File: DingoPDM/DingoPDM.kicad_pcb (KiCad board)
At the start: 4 copper layers, 72.4 x 95.2 mm, 156 parts, among them J1 RedCubeTerminal, J2 RedCubeTerminal, J3 Conn_01x12, J4 TC, J5 USB_C_Receptacle_USB2.0, SW1 BOOT, U1 VXO7805-500-M, U10 BTS7008-2EPA, U11 BTS7008-2EPA, U12 LM324, U13 BTS7008-2EPA, U14 OKI-78SR-5_1.5-W36H-C, U15 TSR_1-2450, U2 LD1117S33CTR, U3 PCA82C250, U4 STM32F446RETx, U5 MB85RC256V, U6 MCP9808, U7 LM324, U8 BTS700n-1EPP, U9 BTS700n-1EPP, Y1 8mHz

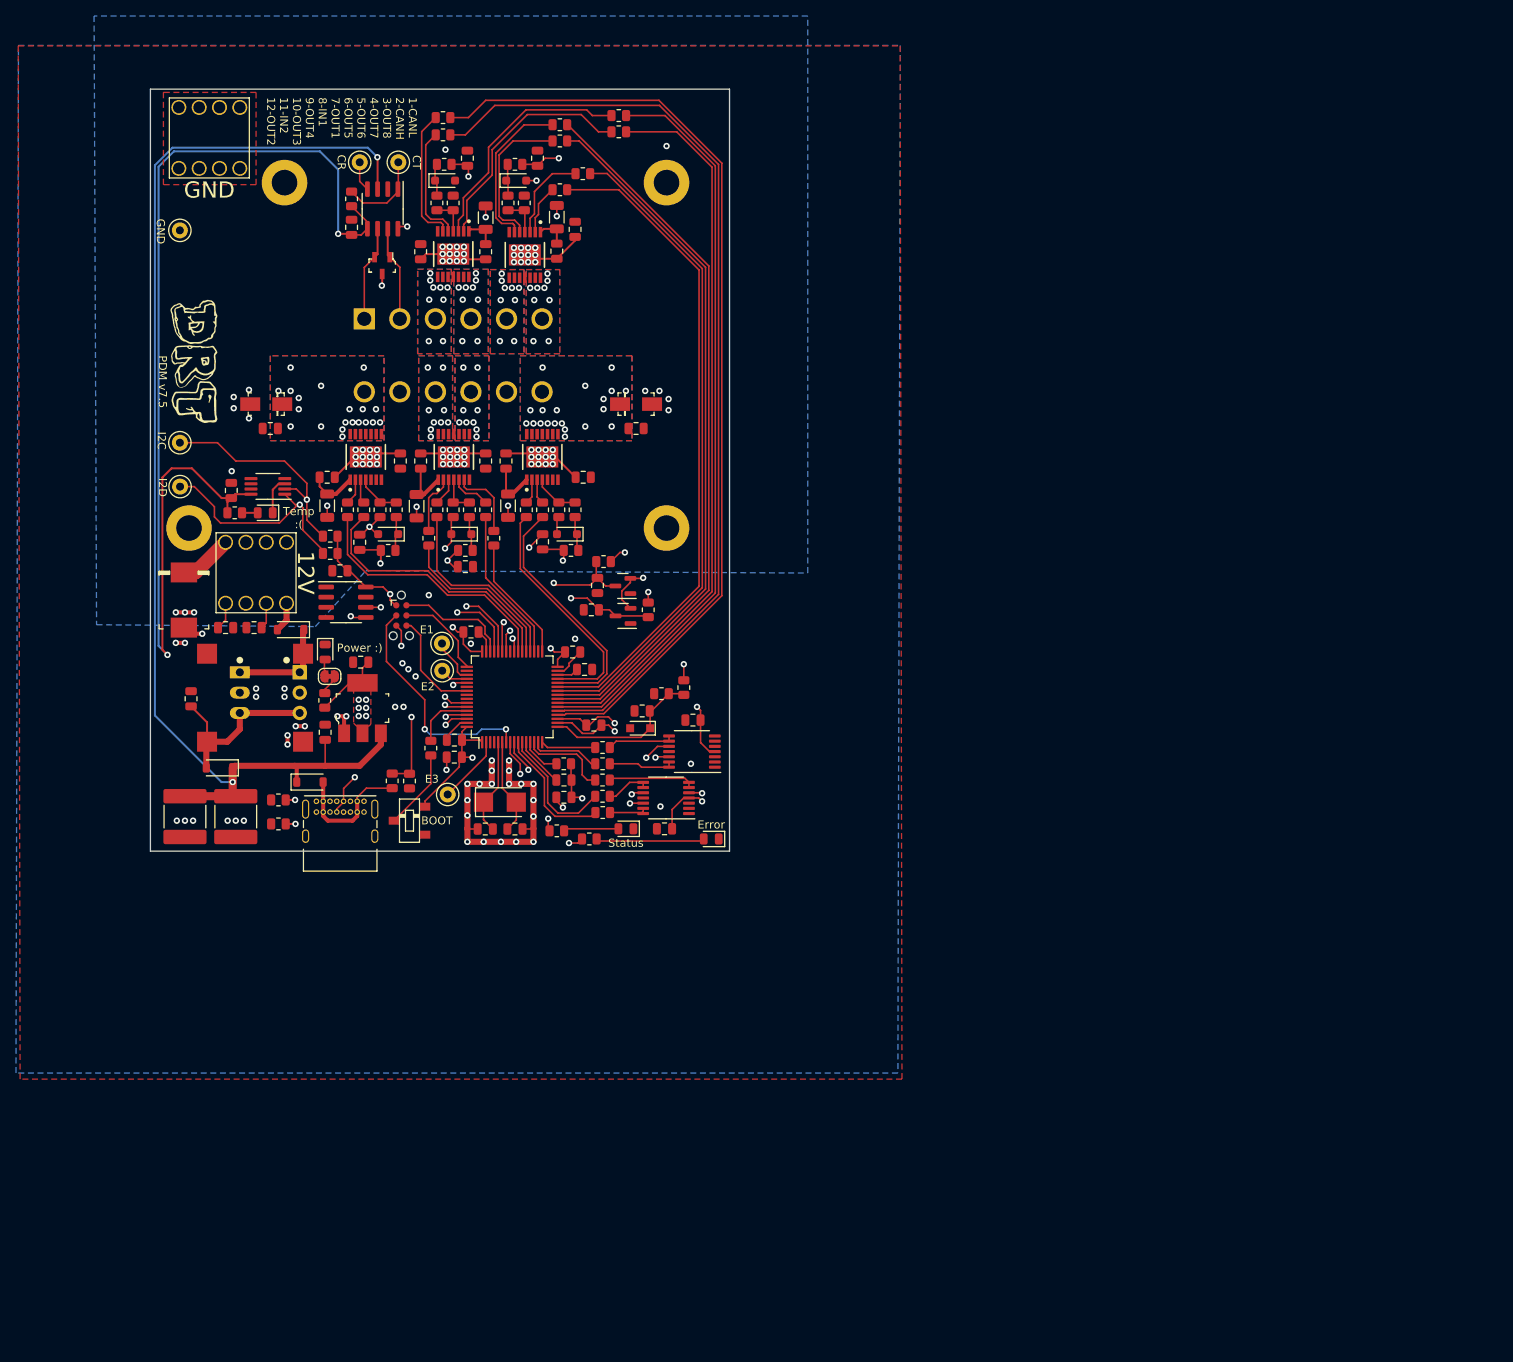
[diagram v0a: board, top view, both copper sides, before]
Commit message: Modified PCB for 10ch PDM board
I modified the original dingoPDM for 10 channels. The board has been manufactured, tested and works but after mounting I decided that it doesn't suit my needs for the current build. I may develop it further in the future, make it pretty etc but for now I am marking this project as stale.
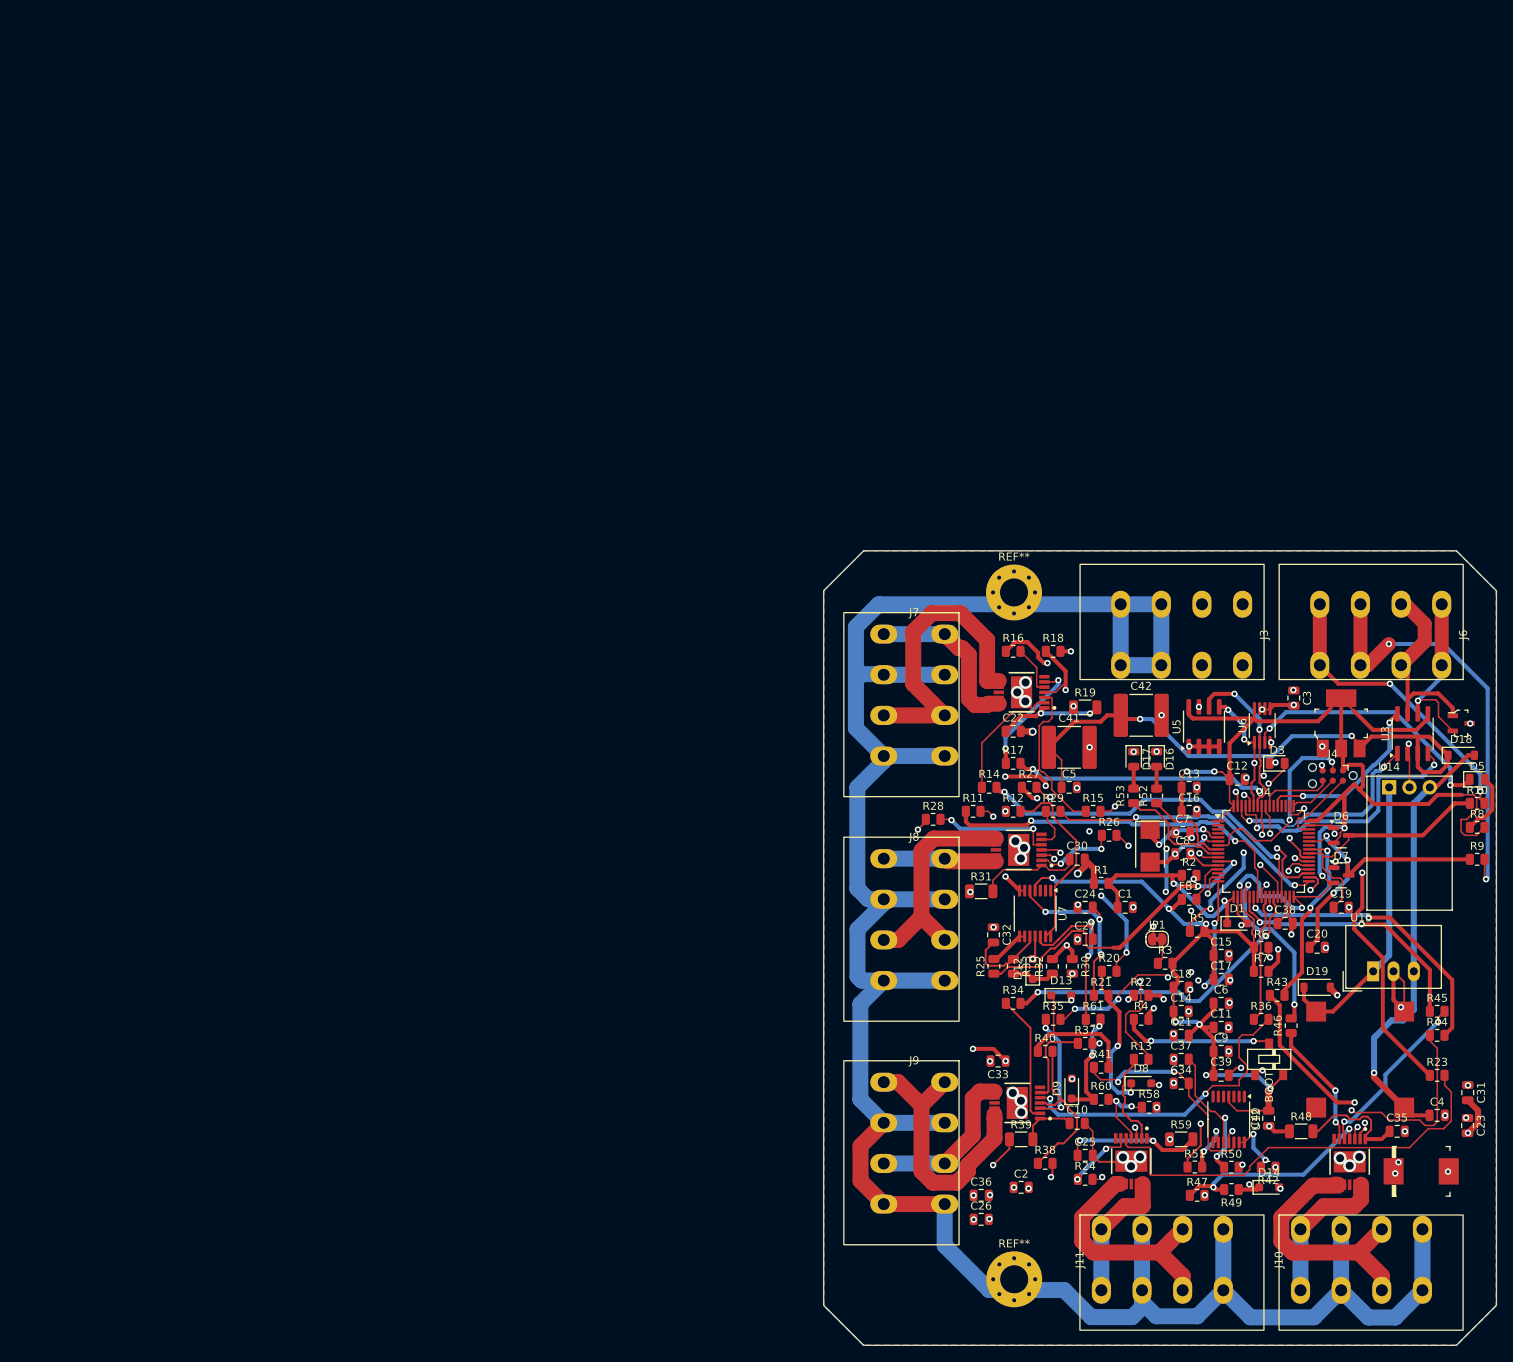
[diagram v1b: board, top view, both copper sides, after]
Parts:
- removed C28: 10nF, Capacitor_SMD:C_0805_2012Metric
- removed C29: 220pF, Capacitor_SMD:C_0805_2012Metric
- removed D10: BYG23M, dingoPDM:DO-214AC
- removed D11: 3.3V, Diode_SMD:D_SOD-323_HandSoldering
- removed D15: Schottky, Diode_SMD:D_SOD-123
- removed G1: DRT_Logo, dingoPDM:DRTLogo
- removed G2: DingoFace, dingoPDM:DingoFaceNoFill
- removed H1, H2, H3, H4: M3, MountingHole:MountingHole_3.2mm_M3_ISO7380_Pad
- removed J1, J2: RedCubeTerminal, dingoPDM:M6_Hole_8Pin_7461084
- removed J5: USB_C_Receptacle_USB2.0, Connector_USB:USB_C_Receptacle_GCT_USB4085
- removed R54, R55: 5.1K, Resistor_SMD:R_0805_2012Metric
- removed R56: 4.7K, Resistor_SMD:R_0805_2012Metric
- removed R57: 10K, Resistor_SMD:R_0805_2012Metric
- removed TP1: GND, TestPoint:TestPoint_Keystone_5000-5004_Miniature
- removed TP10: E3, TestPoint:TestPoint_Keystone_5000-5004_Miniature
- removed TP2: CAN_T, TestPoint:TestPoint_Keystone_5000-5004_Miniature
- removed TP3: CAN_R, TestPoint:TestPoint_Keystone_5000-5004_Miniature
- removed TP5: I2C1_SCL, TestPoint:TestPoint_Keystone_5000-5004_Miniature
- removed TP6: I2C1_SDA, TestPoint:TestPoint_Keystone_5000-5004_Miniature
- removed TP8: E1, TestPoint:TestPoint_Keystone_5000-5004_Miniature
- removed TP9: E2, TestPoint:TestPoint_Keystone_5000-5004_Miniature
- added J10: out7_8, DF_Conn:DIP-8_300_ELL, F.Cu at (113.5, 113.1)
- added J11: out9_10, DF_Conn:DIP-8_300_ELL, F.Cu at (88.6, 113.1)
- added J6: conn_comms, DF_Conn:DIP-8_300_ELL, F.Cu at (116.0, 34.9)
- added J7: out1_2, DF_Conn:DIP-8_300_ELL, F.Cu at (57.6, 42.5)
- added J8: out3_4, DF_Conn:DIP-8_300_ELL, F.Cu at (57.6, 70.5)
- added J9: out5_6, DF_Conn:DIP-8_300_ELL, F.Cu at (57.6, 98.5)
- added R58: 1.2K, Resistor_SMD:R_0805_2012Metric, F.Cu at (87.0, 94.0)
- added R59: 47R 1/4W, Resistor_SMD:R_1206_3216Metric, F.Cu at (91.0, 98.0)
- added R60: 4.7K, Resistor_SMD:R_0805_2012Metric, F.Cu at (81.0, 93.0)
- added R61: 4.7K, Resistor_SMD:R_0805_2012Metric, F.Cu at (80.0, 83.0)
- added REF**: MountingHole_3.5mm_Pad_Via, MountingHole:MountingHole_3.5mm_Pad_Via, F.Cu at (70.1, 115.5)
- added REF**: MountingHole_3.5mm_Pad_Via, MountingHole:MountingHole_3.5mm_Pad_Via, F.Cu at (70.1, 29.6)
- C24: value 10nF -> 220pF
- C25: value 220pF -> 47nF
- C26: value 47nF -> 100nF
- C27: value 100nF -> 220pF
- D8: value BYG23M -> 3.3V; footprint dingoPDM:DO-214AC -> Diode_SMD:D_SOD-323_HandSoldering
- J3: value Conn_01x12 -> batt; footprint dingoPDM:DT15-12PA -> DF_Conn:DIP-8_300_ELL
- R15, R21: value 1.2K -> 4.7K
- R16, R22: value 47R 1/4W -> 4.7K; footprint Resistor_SMD:R_1206_3216Metric -> Resistor_SMD:R_0805_2012Metric
- R18: value 4.7K -> 1.2K
- R19: value 4.7K -> 47R 1/4W; footprint Resistor_SMD:R_0805_2012Metric -> Resistor_SMD:R_1206_3216Metric
- U14: footprint dingoPDM:Converter_DCDC_Murata_OKI-78SR_Horizontal -> Converter_DCDC:Converter_DCDC_Murata_OKI-78SR_Horizontal
- U15: footprint dingoPDM:Converter_DCDC_TRACO_TSR-1_THT -> Converter_DCDC:Converter_DCDC_TRACO_TSR-1_THT
- U8, U9: value BTS700n-1EPP -> BTS7008-2EPA
- moved D2 170.3 mm to (121.0, 102.0), turned to 0 degrees
- moved R45 165.7 mm to (123.0, 82.0), turned to 0 degrees
- moved C4 164.2 mm to (123.0, 95.0), turned to 0 degrees
- moved D14 162.6 mm to (102.0, 104.0)
- moved R8 160.2 mm to (128.0, 59.0), turned to 0 degrees
- moved U13 159.5 mm to (112.1, 100.8)
- moved R50 159.4 mm to (97.3, 101.5), turned to 0 degrees
- moved R49 158.3 mm to (97.3, 104.3), turned to 180 degrees
- moved C35 158.3 mm to (118.0, 97.0), turned to 0 degrees
- moved R46 155.3 mm to (104.7, 83.8), turned to 90 degrees
- moved D18 155.2 mm to (126.0, 50.0), turned to 0 degrees
- moved D5 155.1 mm to (128.0, 53.0), turned to 0 degrees
- moved R47 155.0 mm to (93.0, 105.0), turned to 0 degrees
- moved R44 153.9 mm to (123.0, 85.0)
- moved R48 153.1 mm to (106.0, 97.0), turned to 0 degrees
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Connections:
- net PF_IS2 renamed PF_IS9_10
- C22 pad 1: Net-(U8-GND) -> Net-(U9-GND)
- C24 pad 2: PF_OUT1 -> /MedCurrentDrivers-added/Sheet5F5A9674/IS
- C25 pad 1: GND -> Net-(U8-GND)
- C25 pad 2: /HighCurrentDrivers/sheet5F5A40B9/IS -> +12V
- C26 pad 1: Net-(U9-GND) -> GND
- C27 pad 2: +12V -> /MedCurrentDrivers-added/Sheet5F5A9675/IS
- J3 pad 1: CAN_L -> +12V
- J3 pad 2: CAN_H -> +12V
- J3 pad 3: PF_OUT8 -> GND
- J3 pad 4: PF_OUT7 -> GND
- R11 pad 1: PF_IS1 -> PF_IS1_2
- R13 pad 2: PF_IN1 -> PF_IN9
- R14 pad 1: Net-(U8-DEN) -> Net-(U9-IN0)
- R14 pad 2: PF_DEN1 -> PF_IN1
- R15 pad 1: Net-(U8-IS) -> Net-(U9-DEN)
- R15 pad 2: GND -> PF_DEN1_2
- R16 pad 1: GND -> PF_DSEL1_2
- R16 pad 2: Net-(U8-GND) -> Net-(U9-DSEL)
- R17 pad 1: Net-(D9-K) -> Net-(U9-IN1)
- R17 pad 2: Net-(U8-IS) -> PF_IN2
- R18 pad 1: /HighCurrentDrivers/sheet5F5A40B9/IS -> Net-(U9-IS)
- R18 pad 2: Net-(D9-K) -> GND
- R19 pad 1: Net-(U9-IN) -> GND
- R19 pad 2: PF_IN2 -> Net-(U9-GND)
- R20 pad 1: Net-(U9-DEN) -> Net-(D8-K)
- R20 pad 2: PF_DEN2 -> Net-(U9-IS)
- R21 pad 1: Net-(U9-IS) -> /MedCurrentDrivers-added/Sheet5F5A9674/IS
- R21 pad 2: GND -> Net-(D8-K)
- R22 pad 1: GND -> Net-(U8-DEN)
- R22 pad 2: Net-(U9-GND) -> PF_DEN9_10
- R23 pad 1: Net-(D11-K) -> PF_DSEL9_10
- R23 pad 2: Net-(U9-IS) -> Net-(U8-DSEL)
- R24 pad 1: /HighCurrentDrivers/sheet5F5A40BA/IS -> Net-(U8-IN1)
- R24 pad 2: Net-(D11-K) -> PF_IN10
- U4 pad 14: PF_IS1 -> unconnected-(U4-PA0-Pad14)
- U4 pad 2: Net-(U4-PC13) -> unconnected-(U4-PC13-Pad2)
- U4 pad 23: PF_IN7 -> PF_IS1_2
- U4 pad 28: PF_DEN1 -> PF_DEN1_2
- U4 pad 34: unconnected-(U4-PB13-Pad34) -> PF_DEN9_10
- U4 pad 38: PF_DEN2 -> PF_DSEL1_2
- U4 pad 41: unconnected-(U4-PA8-Pad41) -> PF_IN7
- U4 pad 42: USB_VBUS -> unconnected-(U4-PA9-Pad42)
- U4 pad 44: USB_D- -> unconnected-(U4-PA11-Pad44)
- U4 pad 45: USB_D+ -> unconnected-(U4-PA12-Pad45)
- U4 pad 50: unconnected-(U4-PA15-Pad50) -> PF_DSEL9_10
- U4 pad 51: Net-(U4-PC10) -> unconnected-(U4-PC10-Pad51)
- U4 pad 52: Net-(U4-PC11) -> unconnected-(U4-PC11-Pad52)
- U4 pad 56: unconnected-(U4-PB4-Pad56) -> PF_IN9
- U4 pad 57: unconnected-(U4-PB5-Pad57) -> PF_IN10
- U7 pad 12: /HighCurrentDrivers/sheet5F5A40BA/IS -> /MedCurrentDrivers-added/Sheet5F5A9675/IS
- U7 pad 5: /HighCurrentDrivers/sheet5F5A40B9/IS -> /MedCurrentDrivers-added/Sheet5F5A9674/IS
- U8 pad 10: PF_OUT1 -> PF_OUT10
- U8 pad 11: PF_OUT1 -> unconnected-(U8-NC4-Pad11)
- U8 pad 12: PF_OUT1 -> PF_OUT9
- U8 pad 13: PF_OUT1 -> PF_OUT9
- U8 pad 14: PF_OUT1 -> PF_OUT9
- U8 pad 5: unconnected-(U8-NC1-Pad5) -> Net-(U8-DSEL)
- U8 pad 6: unconnected-(U8-NC2-Pad6) -> Net-(U8-IN1)
- U8 pad 8: PF_OUT1 -> PF_OUT10
- U8 pad 9: PF_OUT1 -> PF_OUT10
- U9 pad 11: PF_OUT2 -> unconnected-(U9-NC4-Pad11)
- U9 pad 12: PF_OUT2 -> PF_OUT1
- U9 pad 13: PF_OUT2 -> PF_OUT1
- U9 pad 14: PF_OUT2 -> PF_OUT1
- U9 pad 2: Net-(U9-IN) -> Net-(U9-IN0)
- U9 pad 5: unconnected-(U9-NC1-Pad5) -> Net-(U9-DSEL)
- U9 pad 6: unconnected-(U9-NC2-Pad6) -> Net-(U9-IN1)
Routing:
- net GND: track 104.0 -> 408.4 mm, vias 71 -> 70
- net +12V: track 97.3 -> 213.8 mm, vias 61 -> 27
- net PF_IN8: track 118.8 -> 22.4 mm, vias 0 -> 2
- net PF_DSEL7_8: track 118.0 -> 32.7 mm, vias 0 -> 2
- net /MedCurrentDrivers/Sheet5F5A9676/IS: track 101.1 -> 20.0 mm
- net +5V: track 151.8 -> 72.3 mm
- net PF_DSEL5_6: track 88.0 -> 16.2 mm
- net /MCU/CAN_STANDBY: track 92.6 -> 22.4 mm
- net PF_IN7: track 90.7 -> 22.9 mm, vias 0 -> 2
- net /MedCurrentDrivers/Sheet5F5A9675/IS: track 95.5 -> 27.6 mm
- net /MCU/CAN_TX: track 113.0 -> 48.9 mm, vias 1 -> 4
- net /HighCurrentDrivers/sheet5F5A40BA/IS: track 62.2 -> 0.00 mm, vias 2 -> 0
- net /MCU/CAN_RX: track 95.7 -> 34.1 mm, vias 1 -> 2
- net PF_DSEL1_2: track 0.00 -> 60.9 mm, vias 0 -> 2
- net PF_IN10: track 0.00 -> 59.3 mm, vias 0 -> 4
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- added copper zone on In1.Cu, net +12V
- added copper zone on In2.Cu, net +12V
- added copper zone on B.Cu, net GND
- removed copper zone on B.Cu, net +12V
- removed copper zone on B.Cu, net +3V3
- removed copper zone on F.Cu, net +3V3
- removed copper zone on In1.Cu, net GND
- removed copper zone on B.Cu, net PF_OUT1
- removed copper zone on F.Cu, net PF_OUT1
- removed copper zone on In1.Cu, net PF_OUT1
- removed copper zone on In2.Cu, net PF_OUT1
- removed copper zone on B.Cu, net PF_OUT2
- removed copper zone on F.Cu, net PF_OUT2
- removed copper zone on In1.Cu, net PF_OUT2
- removed copper zone on In2.Cu, net PF_OUT2
- removed copper zone on B.Cu, net PF_OUT3
- removed copper zone on F.Cu, net PF_OUT3
- removed copper zone on In1.Cu, net PF_OUT3
- removed copper zone on In2.Cu, net PF_OUT3
- removed copper zone on B.Cu, net PF_OUT4
- removed copper zone on F.Cu, net PF_OUT4
- removed copper zone on In1.Cu, net PF_OUT4
- removed copper zone on In2.Cu, net PF_OUT4
- removed copper zone on B.Cu, net PF_OUT5
- removed copper zone on F.Cu, net PF_OUT5
- removed copper zone on In1.Cu, net PF_OUT5
- removed copper zone on In2.Cu, net PF_OUT5
- removed copper zone on B.Cu, net PF_OUT6
- removed copper zone on F.Cu, net PF_OUT6
- removed copper zone on In1.Cu, net PF_OUT6
- removed copper zone on In2.Cu, net PF_OUT6
- removed copper zone on B.Cu, net PF_OUT7
- removed copper zone on F.Cu, net PF_OUT7
- removed copper zone on In1.Cu, net PF_OUT7
- removed copper zone on In2.Cu, net PF_OUT7
- removed copper zone on B.Cu, net PF_OUT8
- removed copper zone on F.Cu, net PF_OUT8
- removed copper zone on In1.Cu, net PF_OUT8
- removed copper zone on In2.Cu, net PF_OUT8
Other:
- board size 72.4 x 95.2 mm -> 84.1 x 99.3 mm
- board text removed: "1-CANL 2-CANH 3-OUT8 4-OUT7 5-OUT6 6-OUT5 7-OUT1 8-IN1 9-OUT4 10-OUT3 11-IN2 12-OUT2"
- board text removed: "12V"
- board text removed: "CR"
- board text removed: "CT"
- board text removed: "Error"
- board text removed: "GND"
- board text removed: "I2C"
- board text removed: "I2D"
- board text removed: "PDM v7.5"
- board text removed: "Power :)"
- board text removed: "SUP"
- board text removed: "Status"
- board text removed: "Temp :("
